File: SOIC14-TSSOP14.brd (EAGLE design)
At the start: 20 x 20.3 mm, 7 parts

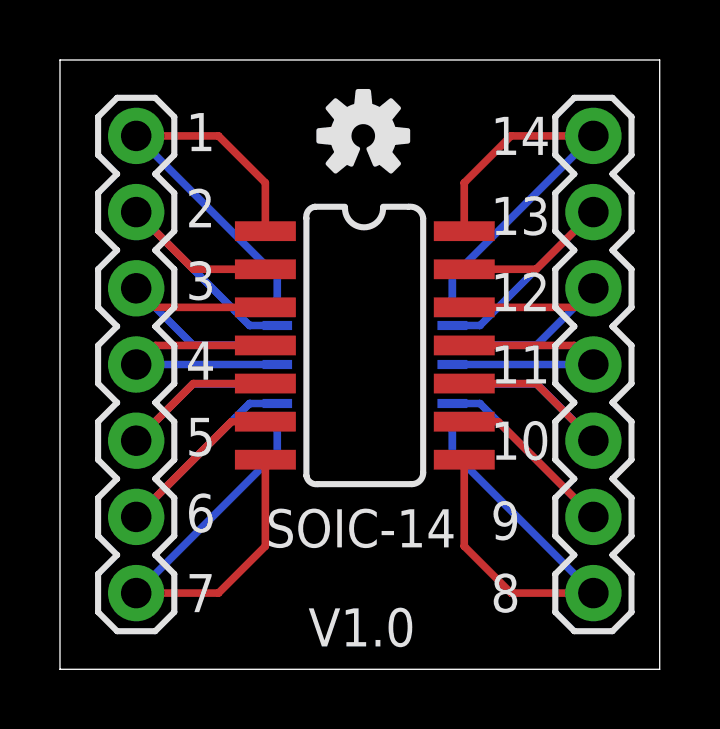
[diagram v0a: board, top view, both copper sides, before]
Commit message: Silk and board revision
Worked several silk screen issues and narrowed some boards.
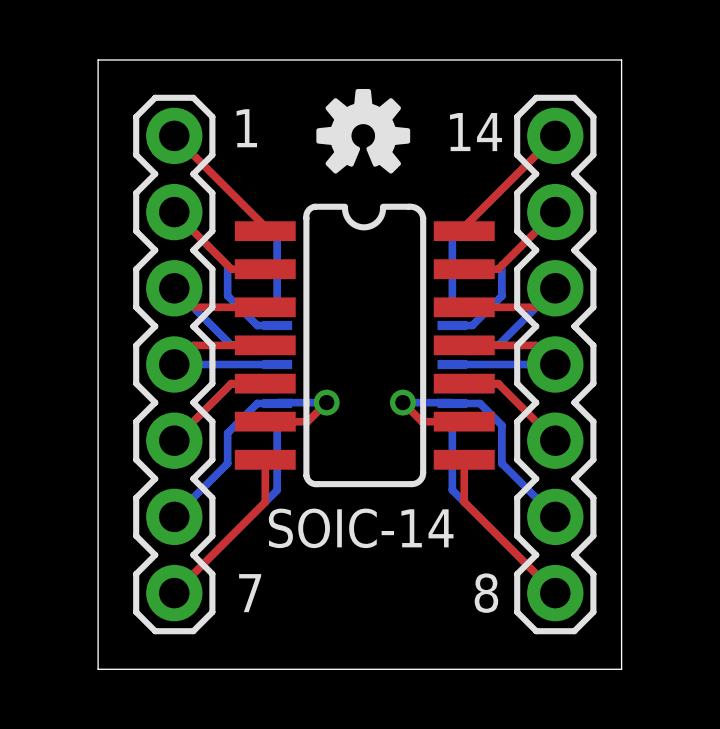
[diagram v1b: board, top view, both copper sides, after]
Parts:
- moved JP1 1.27 mm to (3.81, 10.2)
- moved JP2 1.27 mm to (16.5, 10.2)
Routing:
- net N$7: track 15.5 -> 12.8 mm
- net N$11: track 14.2 -> 11.5 mm
- net N$1: track 14.2 -> 11.5 mm
- net N$17: track 15.5 -> 12.8 mm
- net N$5: track 10.6 -> 8.04 mm
- net N$4: track 9.27 -> 6.73 mm
- net N$3: track 10.1 -> 7.51 mm
- net N$13: track 10.1 -> 7.51 mm
- net N$15: track 10.6 -> 8.04 mm
- net N$14: track 9.27 -> 6.73 mm
- net N$6: track 11.9 -> 9.56 mm, vias 0 -> 1
- net N$16: track 11.9 -> 9.71 mm, vias 0 -> 1
- net N$2: track 11.4 -> 9.42 mm
- net N$12: track 11.4 -> 9.42 mm
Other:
- board size 20 x 20.3 mm -> 17.4 x 20.3 mm
- board text removed: "10"
- board text removed: "11"
- board text removed: "12"
- board text removed: "13"
- board text removed: "2"
- board text removed: "3"
- board text removed: "4"
- board text removed: "5"
- board text removed: "6"
- board text removed: "9"
- board text removed: "V1.0"
